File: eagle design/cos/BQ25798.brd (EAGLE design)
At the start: 160 x 100 mm, 42 parts, among them IC1 CSD17581Q3A, IC2 CSD17581Q3A, IC3 CSD17581Q3A, IC4 CSD17581Q3A, IC5 PQ25798RQMT, IC6 CSD17581Q3A

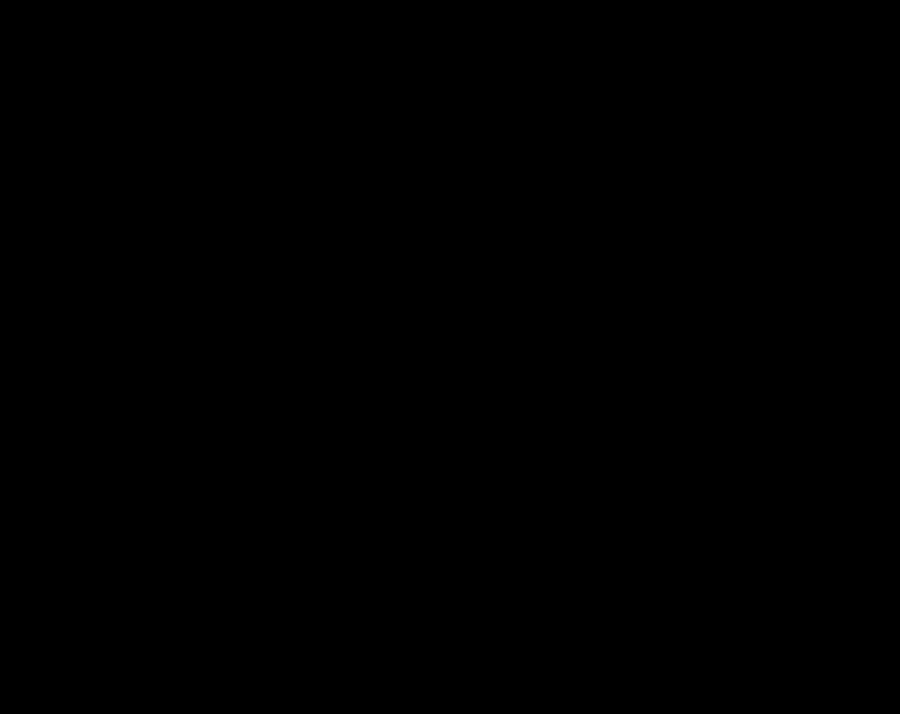
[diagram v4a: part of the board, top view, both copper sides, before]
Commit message: - added USB mini B connector (MX-67503-1230 USB Mini-B SMT straight socket.lbr)
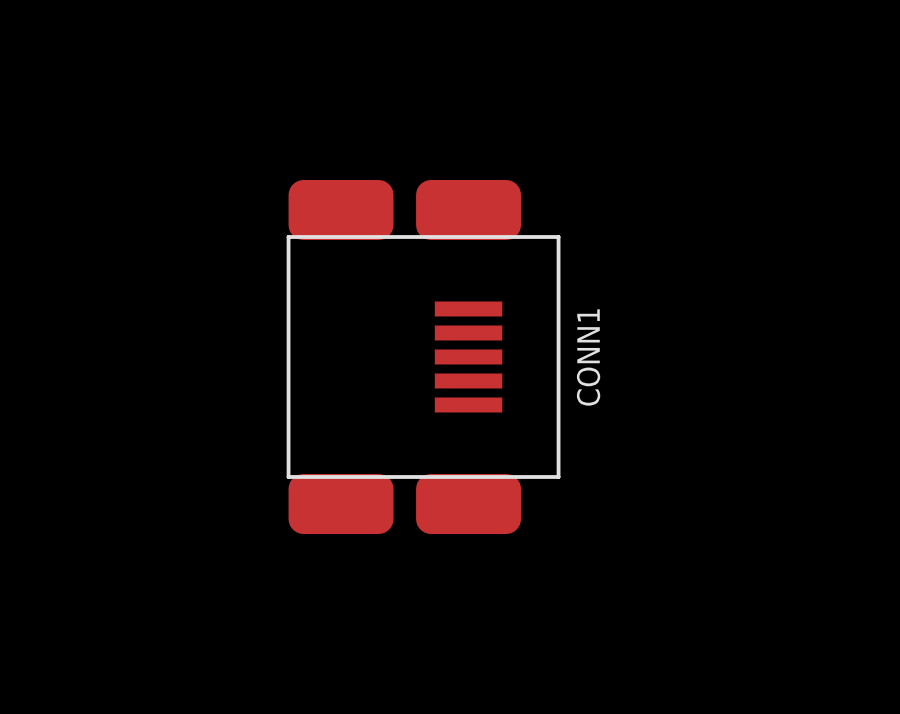
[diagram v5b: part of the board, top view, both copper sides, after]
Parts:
- added CONN1: MX-67503-1230, MX-67503-1230 USB Mini-B SMT straight socket:SMT
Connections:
- net GND: now also CONN1.GND1, CONN1.GND2, CONN1.GND3, CONN1.GND4, CONN1.GND5
- net USB_D+: now also CONN1.D+
- net USB_D-: now also CONN1.D-
- net V_USB: now also CONN1.VBUS
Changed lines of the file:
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@@
 <attribute name="VALUE" x="-12.75" y="-58.5" size="0.75" layer="27" font="vector" rot="R270" align="center"/>
+</element>
+<element name="CONN1" library="MX-67503-1230 USB Mini-B SMT straight socket" package="SMT" value="MX-67503-1230" x="-23" y="16" smashed="yes">
+<attribute name="NAME" x="-19" y="16" size="0.75" layer="25" font="vector" rot="R90" align="center"/>
+<attribute name="VALUE" x="-19" y="12" size="1.27" layer="27"/>
 </element>
 </elements>
@@
 <contactref element="IC5" pad="27_GND"/>
 <contactref element="BATT2" pad="-"/>
-<wire x1="-85" y1="50.35" x2="-59.5" y2="50.15" width="0" layer="19" extent="1-1"/>
-<wire x1="19.4" y1="-59.5" x2="-85" y2="50.35" width="0" layer="19" extent="1-1"/>
+<contactref element="CONN1" pad="GND5"/>
+<contactref element="CONN1" pad="GND4"/>
+<contactref element="CONN1" pad="GND3"/>
+<contactref element="CONN1" pad="GND2"/>
+<contactref element="CONN1" pad="GND1"/>
+<wire x1="-23" y1="11.1" x2="-27.25" y2="11.1" width="0" layer="19" extent="1-1"/>
+<wire x1="-23" y1="14.4" x2="-23" y2="11.1" width="0" layer="19" extent="1-1"/>
+<wire x1="-23" y1="20.9" x2="-23" y2="14.4" width="0" layer="19" extent="1-1"/>
+<wire x1="-27.25" y1="20.9" x2="-23" y2="20.9" width="0" layer="19" extent="1-1"/>
+<wire x1="-36.45" y1="-87.5" x2="-23" y2="20.9" width="0" layer="19" extent="1-1"/>
+<wire x1="-10" y1="-64.77" x2="-36.45" y2="-87.5" width="0" layer="19" extent="1-1"/>
+<wire x1="1.4" y1="-57" x2="-10" y2="-64.77" width="0" layer="19" extent="1-1"/>
+<wire x1="1.4" y1="-50.5" x2="1.4" y2="-57" width="0" layer="19" extent="1-1"/>
+<wire x1="18.65" y1="-55" x2="1.4" y2="-57" width="0" layer="19" extent="1-1"/>
+<wire x1="19.4" y1="-59.5" x2="18.65" y2="-55" width="0" layer="19" extent="1-1"/>
 <wire x1="19.4" y1="-66" x2="19.4" y2="-59.5" width="0" layer="19" extent="1-1"/>
 <wire x1="19.4" y1="-72.5" x2="19.4" y2="-66" width="0" layer="19" extent="1-1"/>
-<wire x1="-85.85" y1="5" x2="19.4" y2="-72.5" width="0" layer="19" extent="1-1"/>
-<wire x1="-85.1" y1="-1" x2="-85.85" y2="5" width="0" layer="19" extent="1-1"/>
-<wire x1="-85.1" y1="-8" x2="-85.1" y2="-1" width="0" layer="19" extent="1-1"/>
-<wire x1="32" y1="-26.45" x2="-85.1" y2="-8" width="0" layer="19" extent="1-1"/>
-<wire x1="36.9" y1="-59.5" x2="32" y2="-26.45" width="0" layer="19" extent="1-1"/>
+<wire x1="36.15" y1="-54.5" x2="19.4" y2="-59.5" width="0" layer="19" extent="1-1"/>
+<wire x1="36.9" y1="-59.5" x2="36.15" y2="-54.5" width="0" layer="19" extent="1-1"/>
 <wire x1="36.9" y1="-66" x2="36.9" y2="-59.5" width="0" layer="19" extent="1-1"/>
 <wire x1="36.9" y1="-72" x2="36.9" y2="-66" width="0" layer="19" extent="1-1"/>
 <wire x1="36.9" y1="-78" x2="36.9" y2="-72" width="0" layer="19" extent="1-1"/>
 <wire x1="36.9" y1="-85" x2="36.9" y2="-78" width="0" layer="19" extent="1-1"/>
-<wire x1="-36.45" y1="-87.5" x2="36.9" y2="-85" width="0" layer="19" extent="1-1"/>
-<wire x1="-10" y1="-64.77" x2="-36.45" y2="-87.5" width="0" layer="19" extent="1-1"/>
-<wire x1="18.65" y1="-55" x2="-59.5" y2="50.15" width="0" layer="19" extent="1-1"/>
-<wire x1="36.15" y1="-54.5" x2="18.65" y2="-55" width="0" layer="19" extent="1-1"/>
-<wire x1="1.4" y1="-57" x2="36.15" y2="-54.5" width="0" layer="19" extent="1-1"/>
-<wire x1="1.4" y1="-50.5" x2="1.4" y2="-57" width="0" layer="19" extent="1-1"/>
-<wire x1="-36.45" y1="-1.5" x2="1.4" y2="-50.5" width="0" layer="19" extent="1-1"/>
-<wire x1="26.5" y1="-9.05" x2="-36.45" y2="-1.5" width="0" layer="19" extent="1-1"/>
-<wire x1="27" y1="-26.45" x2="26.5" y2="-9.05" width="0" layer="19" extent="1-1"/>
-<wire x1="4" y1="5.2" x2="27" y2="-26.45" width="0" layer="19" extent="1-1"/>
+<wire x1="32" y1="-26.45" x2="36.15" y2="-54.5" width="0" layer="19" extent="1-1"/>
+<wire x1="27" y1="-26.45" x2="32" y2="-26.45" width="0" layer="19" extent="1-1"/>
+<wire x1="26.5" y1="-9.05" x2="27" y2="-26.45" width="0" layer="19" extent="1-1"/>
+<wire x1="4" y1="5.2" x2="26.5" y2="-9.05" width="0" layer="19" extent="1-1"/>
+<wire x1="-36.45" y1="-1.5" x2="4" y2="5.2" width="0" layer="19" extent="1-1"/>
+<wire x1="-85.1" y1="-1" x2="-36.45" y2="-1.5" width="0" layer="19" extent="1-1"/>
+<wire x1="-85.85" y1="5" x2="-85.1" y2="-1" width="0" layer="19" extent="1-1"/>
+<wire x1="-85.1" y1="-8" x2="-85.1" y2="-1" width="0" layer="19" extent="1-1"/>
+<wire x1="-85" y1="50.35" x2="-85.85" y2="5" width="0" layer="19" extent="1-1"/>
+<wire x1="-59.5" y1="50.15" x2="-85" y2="50.35" width="0" layer="19" extent="1-1"/>
 </signal>
 <signal name="PROG" class="3">
@@
 <contactref element="C2" pad="1"/>
 <contactref element="C3" pad="1"/>
-<wire x1="-51.025" y1="52.025" x2="-72.525" y2="52.025" width="0" layer="19" extent="1-1"/>
-<wire x1="-87.15" y1="5" x2="-72.525" y2="52.025" width="0" layer="19" extent="1-1"/>
-<wire x1="-87.9" y1="-1" x2="-87.15" y2="5" width="0" layer="19" extent="1-1"/>
-<wire x1="-87.9" y1="-8" x2="-87.9" y2="-1" width="0" layer="19" extent="1-1"/>
-<wire x1="2.1" y1="4.3" x2="-51.025" y2="52.025" width="0" layer="19" extent="1-1"/>
-<wire x1="2.1" y1="4.7" x2="2.1" y2="4.3" width="0" layer="19" extent="1-1"/>
 <contactref element="IC3" pad="6_D"/>
 <contactref element="IC3" pad="7_D"/>
@@
 <contactref element="IC4" pad="8_D"/>
 <contactref element="IC4" pad="9_D"/>
+<wire x1="-87.9" y1="-1" x2="-87.9" y2="-8" width="0" layer="19" extent="1-1"/>
+<wire x1="-87.15" y1="5" x2="-87.9" y2="-1" width="0" layer="19" extent="1-1"/>
+<wire x1="-73.5" y1="50.825" x2="-87.15" y2="5" width="0" layer="19" extent="1-1"/>
+<wire x1="-73.825" y1="52.025" x2="-73.5" y2="50.825" width="0" layer="19" extent="1-1"/>
+<wire x1="-74.475" y1="52.025" x2="-73.825" y2="52.025" width="0" layer="19" extent="1-1"/>
+<wire x1="-73.175" y1="52.025" x2="-73.825" y2="52.025" width="0" layer="19" extent="1-1"/>
+<wire x1="-72.525" y1="52.025" x2="-73.175" y2="52.025" width="0" layer="19" extent="1-1"/>
+<wire x1="-52.975" y1="52.025" x2="-72.525" y2="52.025" width="0" layer="19" extent="1-1"/>
+<wire x1="-52.325" y1="52.025" x2="-52.975" y2="52.025" width="0" layer="19" extent="1-1"/>
+<wire x1="-51.675" y1="52.025" x2="-52.325" y2="52.025" width="0" layer="19" extent="1-1"/>
+<wire x1="-51.025" y1="52.025" x2="-51.675" y2="52.025" width="0" layer="19" extent="1-1"/>
+<wire x1="-52" y1="50.825" x2="-52.325" y2="52.025" width="0" layer="19" extent="1-1"/>
+<wire x1="2.1" y1="4.7" x2="-52" y2="50.825" width="0" layer="19" extent="1-1"/>
+<wire x1="2.1" y1="4.3" x2="2.1" y2="4.7" width="0" layer="19" extent="1-1"/>
 </signal>
 <signal name="SOLAR" class="1">
@@
 <contactref element="IC2" pad="8_D"/>
 <contactref element="IC2" pad="9_D"/>
-<wire x1="-57" y1="51.325" x2="-59.5" y2="48.85" width="0" layer="19" extent="1-1"/>
+<contactref element="CONN1" pad="VBUS"/>
+<wire x1="2.6" y1="1.6" x2="-23" y2="17.6" width="0" layer="19" extent="1-1"/>
+<wire x1="2.25" y1="1.9" x2="2.6" y2="1.6" width="0" layer="19" extent="1-1"/>
+<wire x1="-57" y1="51.325" x2="2.25" y2="1.9" width="0" layer="19" extent="1-1"/>
 <wire x1="-56.675" y1="52.525" x2="-57" y2="51.325" width="0" layer="19" extent="1-1"/>
 <wire x1="-56.025" y1="52.525" x2="-56.675" y2="52.525" width="0" layer="19" extent="1-1"/>
 <wire x1="-57.325" y1="52.525" x2="-56.675" y2="52.525" width="0" layer="19" extent="1-1"/>
 <wire x1="-57.975" y1="52.525" x2="-57.325" y2="52.525" width="0" layer="19" extent="1-1"/>
-<wire x1="2.6" y1="1.6" x2="-56.025" y2="52.525" width="0" layer="19" extent="1-1"/>
-<wire x1="2.25" y1="1.9" x2="2.6" y2="1.6" width="0" layer="19" extent="1-1"/>
+<wire x1="-59.5" y1="48.85" x2="-57" y2="51.325" width="0" layer="19" extent="1-1"/>
 </signal>
 <signal name="I2C_SDA">
@@
 <signal name="USB_D-">
 <contactref element="IC5" pad="7_D-"/>
+<contactref element="CONN1" pad="D-"/>
+<wire x1="2.1" y1="2.7" x2="-23" y2="16.8" width="0" layer="19" extent="1-1"/>
 </signal>
 <signal name="USB_D+">
 <contactref element="IC5" pad="6_D+"/>
+<contactref element="CONN1" pad="D+"/>
+<wire x1="2.1" y1="3.1" x2="-23" y2="16" width="0" layer="19" extent="1-1"/>
 </signal>
 <signal name="BATTERY_MID" class="1">

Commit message: - added 3V3 LMR34206-Q1 - Synchronous Step-Down Converter & associated peripherals
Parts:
- added C21, C22, C23, C24, C25, C26: 10u/50V, rcl:C1206
- added D3, D4: BZT52C2V0T, BZT52C2V0T - Zener diode:SOD-523-2
- added IC7: CSD17581Q3A, CSD17581Q3A - N-MosFET:PQFN-12
- added L2: 74437346068, 74437346022 - Power Inductor:SMD
- added R12: 10k, rcl:R0402
- C1, C13: value 0.1u -> 0.1u/50V
- C10: value 4.7n/50V -> 0.1u/50V; device rcl:C0805 -> rcl:C0402
- C11: value 10u/50V -> 1u/50V; device rcl:C1206 -> rcl:C0805
- C12, C19, C2, C3: value 10u/50V -> 0.1u/50V; device rcl:C1206 -> rcl:C0402
- C14: value 10u/50V -> 47u/16V
- C16: value 10u/50V -> 4.7n/50V; device rcl:C1206 -> rcl:C0805
- C4: value 0.1u -> 4.7n/50V; device rcl:C0402 -> rcl:C0805
- C5: value 0.1u -> 10u/50V; device rcl:C0402 -> rcl:C1206
- C6: value 47n -> 0.1u/50V; device rcl:C0805 -> rcl:C0402
- C7: value 47n/50V -> 10u/50V; device rcl:C0805 -> rcl:C1206
- C8: value 0.1u -> 47n/50V; device rcl:C0402 -> rcl:C0805
- C9: value 10u/50V -> 47n/50V; device rcl:C1206 -> rcl:C0805
- D1, D2: value BZT52C2V0T -> CUHS20S30,H3F; device BZT52C2V0T - Zener diode:SOD-523-2 -> CUHS20S30 - Schottky Barrier Diode:US2H
- IC5: value PQ25798RQMT -> LMR34206SC3QRNXRQ1; device BQ25798 - Battery Charger:QFN29 -> LMR34206-Q1 - Synchronous Step-Down Converter:VQFN-HR(12)
- IC6: value CSD17581Q3A -> PQ25798RQMT; device CSD17581Q3A - N-MosFET:PQFN-12 -> BQ25798 - Battery Charger:QFN29
- R1: value 10k -> 8.2k,0.1%
- R11, R2, R4, R5, R6, R7, R8, R9: device rcl:R0805 -> rcl:R0402
- R3: value 8.2k,0.1% -> 10k; device rcl:R0805 -> rcl:R0402
- moved C4 254.1 mm to (-7.50, -191.0), turned to 270 degrees
- moved D1 244.2 mm to (-5.00, -182.5), turned to 90 degrees
- moved D2 238.0 mm to (-8.50, -182.5)
- moved IC5 197.5 mm to (3.50, -194.0), turned to 270 degrees
- moved C12 150.7 mm to (3.00, -222.5)
- moved C14 140.1 mm to (12.5, -190.0), turned to 270 degrees
- moved C11 134.3 mm to (3.00, -199.5), turned to 270 degrees
- moved C6 127.1 mm to (-5.50, -191.0), turned to 270 degrees
- moved R1 124.3 mm to (-35.5, -1.50), turned to 0 degrees
- moved R3 123.2 mm to (-67.5, -120.5), turned to 90 degrees
- moved C10 108.2 mm to (-4.00, -191.0), turned to 270 degrees
- moved C9 89.2 mm to (-67.5, -85.0)
- moved C8 89.1 mm to (-67.5, -80.0)
- moved C7 79.3 mm to (-86.5, -8.00)
- moved C2 57.3 mm to (-59.5, 49.5), turned to 90 degrees
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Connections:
- new net !PG!: IC5.8_!PG!, R12.2
- new net BOOT: C12.2, IC5.4_BOOT
- new net SW: C12.1, IC5.12_SW, IC5.3_NC, L2.P$1
- new net VCC: C11.1, IC5.5_VCC
- new net VIN: C10.1, C4.1, C6.1, D1.A, D2.A, IC5.10_VIN, IC5.2_VIN, IC5.9_!EN!
- net 3V3: now also C14.1, IC5.7_FB, L2.P$2, R12.1, R3.2; no longer R1.2
- net ACDRV1: now also D4.C, IC6.11_ACDRV1; no longer D2.C, IC5.11_ACDRV1
- net ACDRV2: now also D3.C, IC6.10_ACDRV2; no longer D1.C, IC5.10_ACDRV2
- net BAT: now also IC6.22_BAT, IC6.23_BAT, IC7.1_S, IC7.2_S, IC7.3_S; no longer IC5.22_BAT, IC5.23_BAT, IC6.1_S, IC6.2_S, IC6.3_S
- net BATP: now also IC6.18_BATP; no longer IC5.18_BATP
- net BATTERY_PLUS: now also C20.1, C22.1, D2.C, IC7.5_D, IC7.6_D, IC7.7_D, IC7.8_D, IC7.9_D; no longer C14.1, C16.1, IC6.5_D, IC6.6_D, IC6.7_D, IC6.8_D, IC6.9_D
- net BTST1: now also C8.1, IC6.4_BTST1; no longer C6.1, IC5.4_BTST1
- net BTST2: now also C9.2, IC6.19_BTST2; no longer C7.2, IC5.19_BTST2
- net GND: now also C1.1, C10.2, C16.1, C21.2, C22.2, C23.2, C24.2, C25.2, C26.2, C4.2, C6.2, C7.2, IC5.11_PGND, IC5.1_PGND, IC5.6_AGND, IC6.27_GND, R1.1; no longer C1.2, C10.1, C12.2, C16.2, C4.1, C8.2, C9.2, IC5.27_GND, R3.1
- net I2C_SCL: now also IC6.14_SCL, R4.1; no longer IC5.14_SCL, R2.1
- net I2C_SDA: now also IC6.15_SDA; no longer IC5.15_SDA
- net ILIM_HIZ: now also IC6.17_ILIM_HIZ; no longer IC5.17_ILIM_HIZ
- net PMID: now also C13.1, C15.1, C17.1, C18.1, IC6.29_PMID; no longer C11.1, C12.1, C8.1, C9.1, IC5.29_PMID
- net PQ25798_!CE!: now also IC6.13_!CE!; no longer IC5.13_!CE!
- net PQ25798_!INT!: now also IC6.21_!INT!, R2.1; no longer IC5.21_!INT!, R1.1
- net PQ25798_!QON!: now also IC6.12_!QON!; no longer IC5.12_!QON!
- net PQ25798_STAT: now also IC6.1, IC6.1_STAT, R3.1; no longer IC5.1, IC5.1_STAT, R4.1
- net PROG: now also IC6.20_PROG, R1.2; no longer IC5.20_PROG, R3.2
- net REGN: now also C16.2, IC6.5_REGN; no longer C10.2, IC5.5_REGN
- net SDRV: now also IC6.24, IC6.24_SDRV, IC7.4_G; no longer IC5.24, IC5.24_SDRV, IC6.4_G
- net SOLAR: now also C1.2, IC6.8_VAC2; no longer C4.2, IC5.8_VAC2
- net SW1: now also C8.2, IC6.28_SW1; no longer C6.2, IC5.28_SW1
- net SW2: now also C9.1, IC6.26_SW2; no longer C7.1, IC5.26_SW2
- net SYS: now also C21.1, C23.1, C24.1, C25.1, C26.1, IC6.25_SYS; no longer C13.1, C15.1, C17.1, C18.1, C20.1, IC5.25_SYS
- net TS: now also IC6.16, IC6.16_TS; no longer IC5.16, IC5.16_TS
- net USB_D+: now also IC6.6_D+; no longer IC5.6_D+
- net USB_D-: now also IC6.7_D-; no longer IC5.7_D-
- net VAC1_SOURCE: now also D4.A; no longer D2.A
- net VAC2_SOURCE: now also D3.A; no longer D1.A
- net VBUS: now also C5.1, C7.1, D1.C, IC6.2_VBUS, IC6.3_VBUS; no longer C1.1, C2.1, IC5.2_VBUS, IC5.3_VBUS
- net V_USB: now also C2.1, IC6.9, IC6.9_VAC1; no longer C5.1, IC5.9, IC5.9_VAC1

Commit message: - added MX-67503-1230 USB Mini-B SMT straight socket mini USB receptacle - added test points and current sense resistors for the two inputs, output and battery
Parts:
- removed CONN1: MX-67503-1230, MX-67503-1230 USB Mini-B SMT straight socket:SMT
- added C27, C28: 10u/50V, rcl:C1206
- added R13, R14, R15, R16: 0.01R,1W,0.5%, rcl:R0402
- added TP1, TP2, TP3, TP4, TP5, TP6, TP7, TP8: TPPAD1-13, testpad:P1-13
- added USB1: 67503-1230, MX-67503-1230 USB Mini-B SMT straight socket:SMT
- C10: value 0.1u/50V -> 47n/50V; device rcl:C0402 -> rcl:C0805
- C11: value 1u/50V -> 47n/50V
- C13: value 0.1u/50V -> 1u/50V; device rcl:C0402 -> rcl:C0805
- C14: value 47u/16V -> 0.1u/50V; device rcl:C1206 -> rcl:C0402
- C15, C21: value 10u/50V -> 0.1u/50V; device rcl:C1206 -> rcl:C0402
- C16: value 4.7n/50V -> 47u/16V; device rcl:C0805 -> rcl:C1206
- C18: value 10u/50V -> 4.7n/50V; device rcl:C1206 -> rcl:C0805
- C19: value 0.1u/50V -> 10u/50V; device rcl:C0402 -> rcl:C1206
- C4: value 4.7n/50V -> 1n/50V; device rcl:C0805 -> rcl:C0402
- C5: value 10u/50V -> 1n/50V; device rcl:C1206 -> rcl:C0402
- C6: value 0.1u/50V -> 4.7n/50V; device rcl:C0402 -> rcl:C0805
- C8: value 47n/50V -> 0.1u/50V; device rcl:C0805 -> rcl:C0402
- C9: value 47n/50V -> 10u/50V; device rcl:C0805 -> rcl:C1206
- D3, D4: value BZT52C2V0T -> BZT52C12T-7
- moved C11 354.6 mm to (-237.0, 61.5), turned to 0 degrees
- moved C10 347.3 mm to (-237.0, 66.5), turned to 0 degrees
- moved C9 292.4 mm to (-256.0, 138.5)
- moved C4 265.7 mm to (-270.5, -153.0), turned to 0 degrees
- moved C24 261.0 mm to (-169.5, 89.5)
- moved C18 258.9 mm to (-205.0, 59.0)
- moved C5 241.9 mm to (-270.5, -158.0)
- moved C26 232.7 mm to (-134.0, 74.5)
- moved C25 232.1 mm to (-134.0, 80.5)
- moved C19 230.6 mm to (-151.5, 80.5)
- moved C7 228.7 mm to (-256.0, 145.5)
- moved C17 228.3 mm to (-151.5, 87.0)
- moved C22 228.3 mm to (-169.5, 96.0)
- moved C23 228.3 mm to (-134.0, 87.0)
- moved C21 227.3 mm to (-134.0, 92.0)
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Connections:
- removed net BATTERY_PLUS: BATT1.+, C20.1, C22.1, D2.C, IC7.5_D, IC7.6_D, IC7.7_D, IC7.8_D, IC7.9_D, R10.2
- new net BATTERY_POSITIVE: BATT1.+, R15.1, TP5.TP
- new net BAT_PP: C22.1, C24.1, D2.C, IC7.5_D, IC7.6_D, IC7.7_D, IC7.8_D, IC7.9_D, R10.2, R15.2, TP6.TP
- new net N$8: R16.2, TP8.TP
- new net VAC1: C2.1, IC2.5_D, IC2.6_D, IC2.7_D, IC2.8_D, IC2.9_D, IC6.9, IC6.9_VAC1, R14.2, TP4.TP
- new net VAC2: C1.2, IC1.5_D, IC1.6_D, IC1.7_D, IC1.8_D, IC1.9_D, IC6.8_VAC2, R13.2, TP2.TP
- net 3V3: now also C16.1; no longer C14.1
- net ACDRV1: now also C5.2
- net ACDRV2: now also C4.1
- net BOOT: now also C14.2; no longer C12.2
- net BTST1: now also C10.1; no longer C8.1
- net BTST2: now also C11.2; no longer C9.2
- net GND: now also C12.2, C16.2, C18.1, C27.2, C28.2, C8.2, C9.2, USB1.GND1, USB1.GND2, USB1.GND3, USB1.GND4, USB1.GND5; no longer C10.2, C11.2, C14.2, C16.1, C18.2, C4.2, C5.2, CONN1.GND1, CONN1.GND2, CONN1.GND3, CONN1.GND4, CONN1.GND5
- net PMID: now also C19.1, C20.1; no longer C13.1, C18.1
- net REGN: now also C18.2; no longer C16.2
- net SOLAR: now also R13.1, TP1.TP; no longer C1.2, IC1.5_D, IC1.6_D, IC1.7_D, IC1.8_D, IC1.9_D, IC6.8_VAC2
- net SW: now also C14.1; no longer C12.1
- net SW1: now also C10.2; no longer C8.2
- net SW2: now also C11.1; no longer C9.1
- net SYS: now also C27.1, C28.1, R16.1, TP7.TP; no longer C19.1, C24.1
- net USB_D+: now also USB1.D+; no longer CONN1.D+
- net USB_D-: now also USB1.D-; no longer CONN1.D-
- net VAC1_SOURCE: now also C5.1
- net VAC2_SOURCE: now also C4.2
- net VBUS: now also C9.1; no longer C5.1
- net VCC: now also C13.1; no longer C11.1
- net VIN: now also C12.1, C8.1; no longer C10.1, C4.1
- net V_USB: now also R14.1, TP3.TP, USB1.VBUS; no longer C2.1, CONN1.VBUS, IC2.5_D, IC2.6_D, IC2.7_D, IC2.8_D, IC2.9_D, IC6.9, IC6.9_VAC1
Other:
- board outline removed
